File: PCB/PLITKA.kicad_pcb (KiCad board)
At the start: 2 copper layers, 120.5 x 85.5 mm, 55 parts, among them SW1 MX_SW_HS, SW10 MX_SW_HS, SW11 MX_SW_HS, SW12 MX_SW_HS, SW13 MX_SW_HS, SW14 MX_SW_HS, SW15 MX_SW_HS, SW16 MX_SW_HS, SW17 MX_SW_HS, SW2 MX_SW_HS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

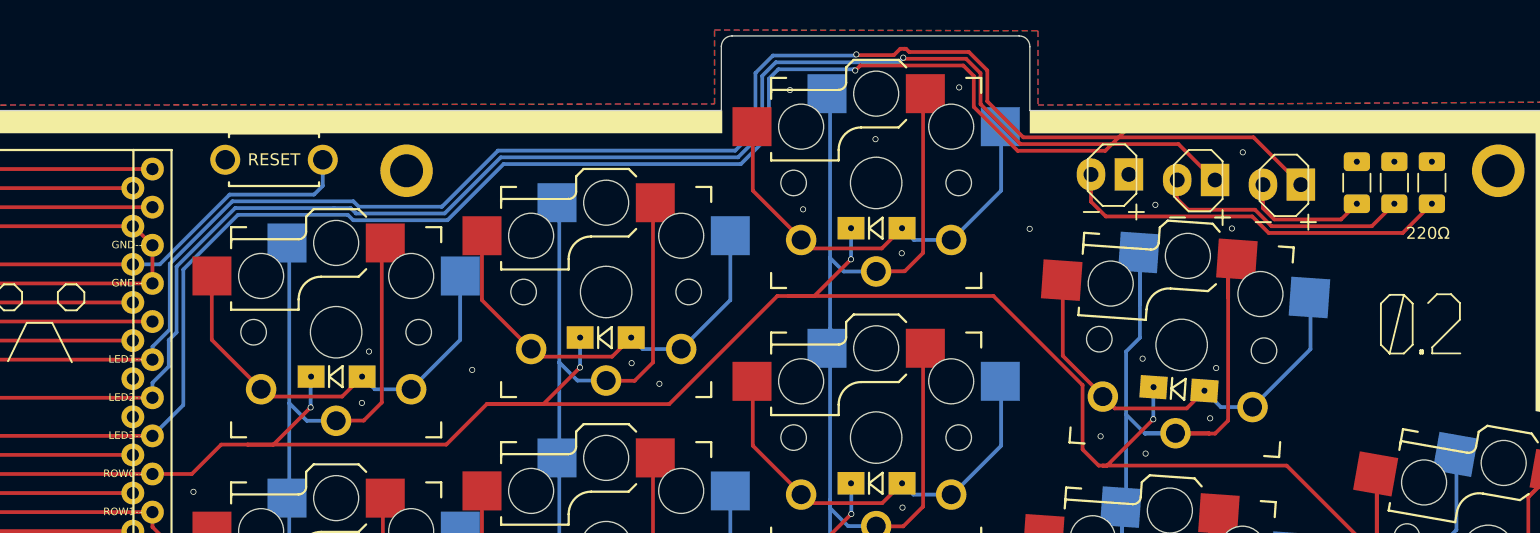
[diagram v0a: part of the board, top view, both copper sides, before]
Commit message: Led removal
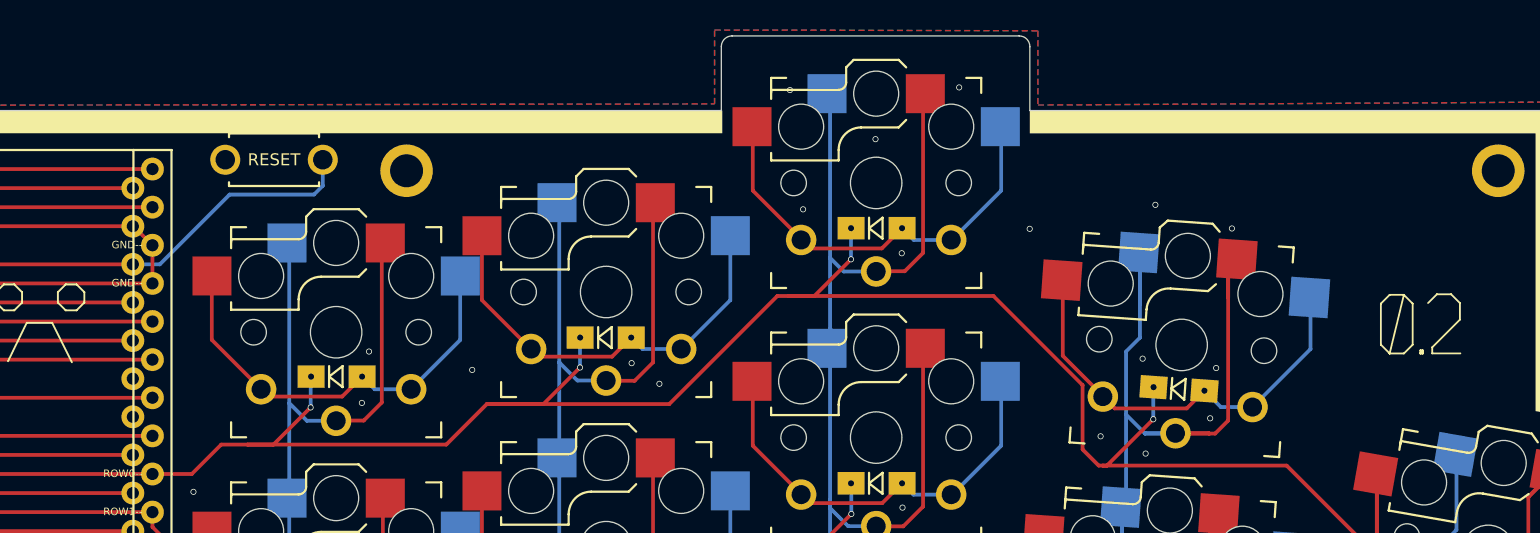
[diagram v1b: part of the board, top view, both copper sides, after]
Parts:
- removed L1, L2, L3: LED, PLITKA:LED_3mm_reversible
- removed R1, R2, R3: 220, PLITKA:R_1206_DoubleSided
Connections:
- U1 pad 6: LED1 -> unconnected-(U1-3/D0/SCL-Pad6)_1
- U1 pad 7: LED2 -> unconnected-(U1-4/D4-Pad7)
- U1 pad 8: LED3 -> unconnected-(U1-5/C6-Pad8)_1
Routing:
- net LED1: track 112.8 -> 0.00 mm, vias 1 -> 0
- net LED2: track 108.5 -> 0.00 mm, vias 1 -> 0
- net LED3: track 104.5 -> 0.00 mm, vias 1 -> 0
- net (no net): track 70.7 -> 121.9 mm
- net /PL3: track 26.2 -> 0.00 mm
- net /PL2: track 17.1 -> 0.00 mm
- net /PL1: track 8.57 -> 0.00 mm
- net GND: vias 63 -> 62
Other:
- board text removed: "220Ω"
- board text removed: "LED1--"
- board text removed: "LED2--"
- board text removed: "LED3--"

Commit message: Tenting puck and the version removal
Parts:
- removed REF**: Tenting Puck, PLITKA:SplitkbTentingPuck_threeholes
